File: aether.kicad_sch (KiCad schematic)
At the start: 41 parts, among them Q1 NPN, Q2 CSD17575Q3, Q3 CSD17575Q3, Q4 CSD17575Q3, Q5 CSD17575Q3, SW1 TDD01H0SB1R, U1 USBLC6-2SC6

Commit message: more routing
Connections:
- net PYRO-TERM_A: now also RN3.5 (R4.2); no longer RN3.8 (R1.2)
- net PYRO-TERM_B: now also RN3.6 (R3.2); no longer RN3.7 (R2.2)
- net PYRO-TERM_C: now also RN3.7 (R2.2); no longer RN3.6 (R3.2)
- net PYRO-TERM_D: now also RN3.8 (R1.2); no longer RN3.5 (R4.2)
- net V-TERM_A: now also RN2.5 (R4.2), RN3.4 (R4.1); no longer RN2.8 (R1.2), RN3.1 (R1.1)
- net V-TERM_B: now also RN2.6 (R3.2), RN3.3 (R3.1); no longer RN2.7 (R2.2), RN3.2 (R2.1)
- net V-TERM_C: now also RN2.7 (R2.2), RN3.2 (R2.1); no longer RN2.6 (R3.2), RN3.3 (R3.1)
- net V-TERM_D: now also RN2.8 (R1.2), RN3.1 (R1.1); no longer RN2.5 (R4.2), RN3.4 (R4.1)
- net at Q5.4 (G), R11.1: now also RN1.4 (R4.1); no longer RN1.1 (R1.1)
- net at Q4.4 (G), R10.1: now also RN1.3 (R3.1); no longer RN1.2 (R2.1)
- net at Q3.4 (G), R9.1: now also RN1.2 (R2.1); no longer RN1.3 (R3.1)
- net at Q2.4 (G), R8.1: now also RN1.1 (R1.1); no longer RN1.4 (R4.1)

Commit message: more routing
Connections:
- net VBUS: now also USB1.A4 (VBUS), USB1.A9 (VBUS), USB1.B4 (VBUS), USB1.B9 (VBUS)
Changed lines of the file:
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@@
+    )
+  )
+  (global_label "VBUS" (shape input) (at 200.66 33.02 0) (fields_autoplaced)
+    (effects (font (size 1.27 1.27)) (justify left))
+    (property "Intersheetrefs" "${INTERSHEET_REFS}" (at 208.5438 33.02 0)
+      (effects (font (size 1.27 1.27)) (justify left) hide)
     )
   )

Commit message: significant amount of routing done
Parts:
- removed SW1: TDD01H0SB1R, TDD01H0SB1R:SOT175P420X230-3N, symbol TDD01H0SB1R:TDD01H0SB1R
- removed SW?: PTS526_SM08_SMTR2_LFS, PTS526_SM08_SMTR2_LFS:SW_PTS526_SM08_SMTR2_LFS, symbol PTS526_SM08_SMTR2_LFS:PTS526_SM08_SMTR2_LFS
- added S1: CJS-1200TA, CJS-1200TA:SW_CJS-1200TA, symbol CJS-1200TA:CJS-1200TA
- added S3: B3U-1000P, B3U-1000P:SW_B3U-1000P, symbol B3U-1000P:B3U-1000P
- D1: footprint LED_SMD:LED_0603_1608Metric -> LED_SMD:LED_0402_1005Metric
- R1, R5: value 10kΩ -> 10k; footprint Resistor_SMD:R_0603_1608Metric -> Resistor_SMD:R_0402_1005Metric
- R10, R11, R8, R9: value 330Ω -> 330
- R2, R3, R4, R6, R7: footprint Resistor_SMD:R_0603_1608Metric -> Resistor_SMD:R_0402_1005Metric
- RGB1: value WS2812B -> WS2812B-2020; footprint LED_SMD:LED_WS2812B_PLCC4_5.0x5.0mm_P3.2mm -> LED_SMD:LED_WS2812B-2020_PLCC4_2.0x2.0mm
- RN1: value 10kΩ -> 10k
- RN2: value 47kΩ -> 47k
- RN3: value 270kΩ -> 270k
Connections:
- net 3.3V: now also S1.3
- net GND: now also S1.1, S3.1
- net PYRO-TERM_A: now also Q5.5 (D), Q5.6 (D), Q5.7 (D), Q5.8 (D), Q5.9 (D), RN3.8 (R1.2); no longer Q2.5 (D), Q2.6 (D), Q2.7 (D), Q2.8 (D), Q2.9 (D), RN3.5 (R4.2)
- net PYRO-TERM_B: now also Q4.5 (D), Q4.6 (D), Q4.7 (D), Q4.8 (D), Q4.9 (D), RN3.7 (R2.2); no longer Q3.5 (D), Q3.6 (D), Q3.7 (D), Q3.8 (D), Q3.9 (D), RN3.6 (R3.2)
- net PYRO-TERM_C: now also Q3.5 (D), Q3.6 (D), Q3.7 (D), Q3.8 (D), Q3.9 (D), RN3.6 (R3.2); no longer Q4.5 (D), Q4.6 (D), Q4.7 (D), Q4.8 (D), Q4.9 (D), RN3.7 (R2.2)
- net PYRO-TERM_D: now also Q2.5 (D), Q2.6 (D), Q2.7 (D), Q2.8 (D), Q2.9 (D), RN3.5 (R4.2); no longer Q5.5 (D), Q5.6 (D), Q5.7 (D), Q5.8 (D), Q5.9 (D), RN3.8 (R1.2)
- net PYRO_A: now also R11.2, STM1.62 (PB9); no longer R8.2
- net PYRO_B: now also R10.2, STM1.61 (PB8); no longer R9.2
- net PYRO_C: now also R9.2, STM1.54 (PD2); no longer R10.2
- net PYRO_D: now also R8.2, STM1.53 (PC12); no longer R11.2
- net STM32-NRST: now also S3.2
- net V-TERM_A: now also RN2.8 (R1.2), RN3.1 (R1.1); no longer RN2.5 (R4.2), RN3.4 (R4.1)
- net V-TERM_B: now also RN2.7 (R2.2), RN3.2 (R2.1); no longer RN2.6 (R3.2), RN3.3 (R3.1)
- net V-TERM_C: now also RN2.6 (R3.2), RN3.3 (R3.1); no longer RN2.7 (R2.2), RN3.2 (R2.1)
- net V-TERM_D: now also RN2.5 (R4.2), RN3.4 (R4.1); no longer RN2.8 (R1.2), RN3.1 (R1.1)
- net at R5.2: now also S1.2
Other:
- moved on the sheet: C12

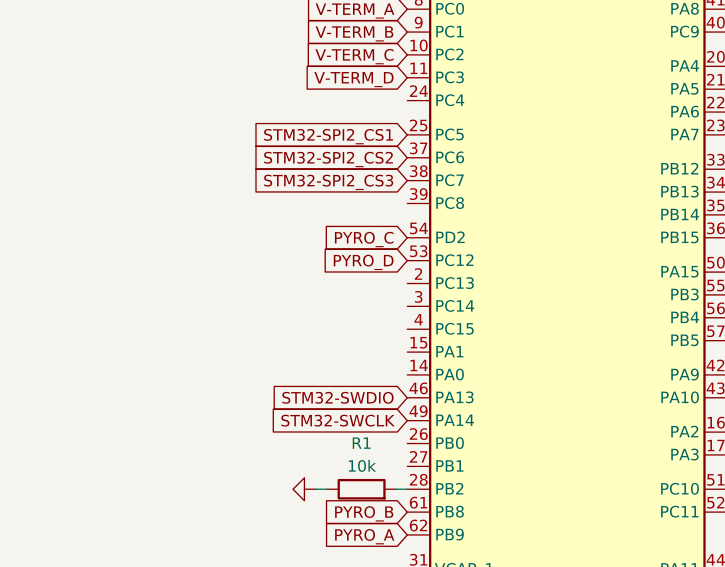
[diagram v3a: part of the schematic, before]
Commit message: signals routed
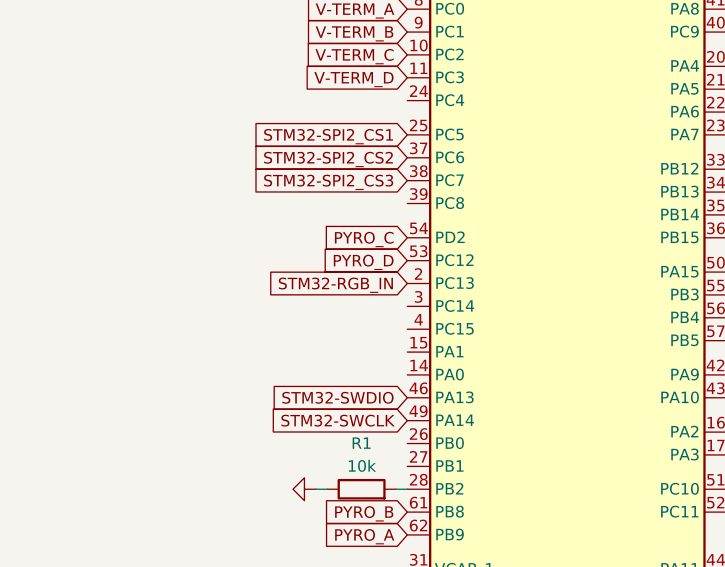
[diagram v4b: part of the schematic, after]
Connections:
- net STM32-RGB_IN: now also STM1.2 (PC13)
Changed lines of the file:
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@@
+    )
+  )
+  (global_label "STM32-RGB_IN" (shape input) (at 43.18 96.52 180) (fields_autoplaced)
+    (effects (font (size 1.27 1.27)) (justify right))
+    (property "Intersheetrefs" "${INTERSHEET_REFS}" (at 25.862 96.52 0)
+      (effects (font (size 1.27 1.27)) (justify right) hide)
     )
   )

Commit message: added power planes
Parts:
- D1: footprint LED_SMD:LED_0402_1005Metric -> LED_SMD:LED_0603_1608Metric
- R1, R2, R3, R4, R5, R6, R7: footprint Resistor_SMD:R_0402_1005Metric -> Resistor_SMD:R_0603_1608Metric
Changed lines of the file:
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@@
       (effects (font (size 1.27 1.27)) (justify left))
     )
-    (property "Footprint" "Resistor_SMD:R_0402_1005Metric" (at 143.002 97.79 90)
+    (property "Footprint" "Resistor_SMD:R_0603_1608Metric" (at 143.002 97.79 90)
       (effects (font (size 1.27 1.27)) hide)
     )
@@
       (effects (font (size 1.27 1.27)))
     )
-    (property "Footprint" "Resistor_SMD:R_0402_1005Metric" (at 204.47 42.418 90)
+    (property "Footprint" "Resistor_SMD:R_0603_1608Metric" (at 204.47 42.418 90)
       (effects (font (size 1.27 1.27)) hide)
     )
@@
       (effects (font (size 1.27 1.27)) (justify right))
     )
-    (property "Footprint" "LED_SMD:LED_0402_1005Metric" (at 186.69 106.68 0)
+    (property "Footprint" "LED_SMD:LED_0603_1608Metric" (at 186.69 106.68 0)
       (effects (font (size 1.27 1.27)) hide)
     )
@@
       (effects (font (size 1.27 1.27)))
     )
-    (property "Footprint" "Resistor_SMD:R_0402_1005Metric" (at 191.77 95.758 90)
+    (property "Footprint" "Resistor_SMD:R_0603_1608Metric" (at 191.77 95.758 90)
       (effects (font (size 1.27 1.27)) hide)
     )
@@
       (effects (font (size 1.27 1.27)) (justify right))
     )
-    (property "Footprint" "Resistor_SMD:R_0402_1005Metric" (at 188.468 99.06 90)
+    (property "Footprint" "Resistor_SMD:R_0603_1608Metric" (at 188.468 99.06 90)
       (effects (font (size 1.27 1.27)) hide)
     )
@@
       (effects (font (size 1.27 1.27)))
     )
-    (property "Footprint" "Resistor_SMD:R_0402_1005Metric" (at 204.47 36.322 90)
+    (property "Footprint" "Resistor_SMD:R_0603_1608Metric" (at 204.47 36.322 90)
       (effects (font (size 1.27 1.27)) hide)
     )
@@
       (effects (font (size 1.27 1.27)))
     )
-    (property "Footprint" "Resistor_SMD:R_0402_1005Metric" (at 38.1 121.158 90)
+    (property "Footprint" "Resistor_SMD:R_0603_1608Metric" (at 38.1 121.158 90)
       (effects (font (size 1.27 1.27)) hide)
     )
@@
       (effects (font (size 1.27 1.27)))
     )
-    (property "Footprint" "Resistor_SMD:R_0402_1005Metric" (at 121.92 139.192 90)
-      (effects (font (size 1.27 1.27)) hide)
-    )
+    (property "Footprint" "Resistor_SMD:R_0603_1608Metric" (at 121.92 139.192 90)
+      (effects (font (size 1.27 1.27)) hide)
+    )
